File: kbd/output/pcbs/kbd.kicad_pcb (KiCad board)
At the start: 2 copper layers, 168.7 x 132.5 mm, 61 parts

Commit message: added mounting holes
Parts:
- added H1: , ceoloide:mounting_hole_plated, F.Cu at (207.5, 164.8)
- added H2: , ceoloide:mounting_hole_plated, F.Cu at (274.4, 180.3)
- added H3: , ceoloide:mounting_hole_plated, F.Cu at (140.5, 159.5)
- added H4: , ceoloide:mounting_hole_plated, F.Cu at (162.4, 60.3)
- added H5: , ceoloide:mounting_hole_plated, F.Cu at (212.1, 58.2)
- added H6: , ceoloide:mounting_hole_plated, F.Cu at (280.4, 77.4)
- added H7: , ceoloide:mounting_hole_plated, F.Cu at (229.8, 102.7)
- added H8: , ceoloide:mounting_hole_plated, F.Cu at (184.1, 100.5)
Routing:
- net (no net): track 856.2 -> 1280.0 mm
- net space_cluster: track 4.72 -> 0.00 mm, vias 1 -> 0
- net layer_cluster: track 4.72 -> 0.00 mm, vias 1 -> 0
- net outer_mod: track 4.72 -> 0.00 mm, vias 1 -> 0
- net outer_top: track 4.72 -> 0.00 mm, vias 1 -> 0
- net outer_num: track 4.72 -> 0.00 mm, vias 1 -> 0
- net outer_home: track 4.72 -> 0.00 mm, vias 1 -> 0
- net outer_bottom: track 4.72 -> 0.00 mm, vias 1 -> 0
- net middle_top: track 4.72 -> 0.00 mm, vias 1 -> 0
- net middle_num: track 4.72 -> 0.00 mm, vias 1 -> 0
- net middle_home: track 4.72 -> 0.00 mm, vias 1 -> 0
- net middle_bottom: track 4.72 -> 0.00 mm, vias 1 -> 0
- net ring_mod: track 4.72 -> 0.00 mm, vias 1 -> 0
- net ring_top: track 4.72 -> 0.00 mm, vias 1 -> 0
- net ring_home: track 4.72 -> 0.00 mm, vias 1 -> 0
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
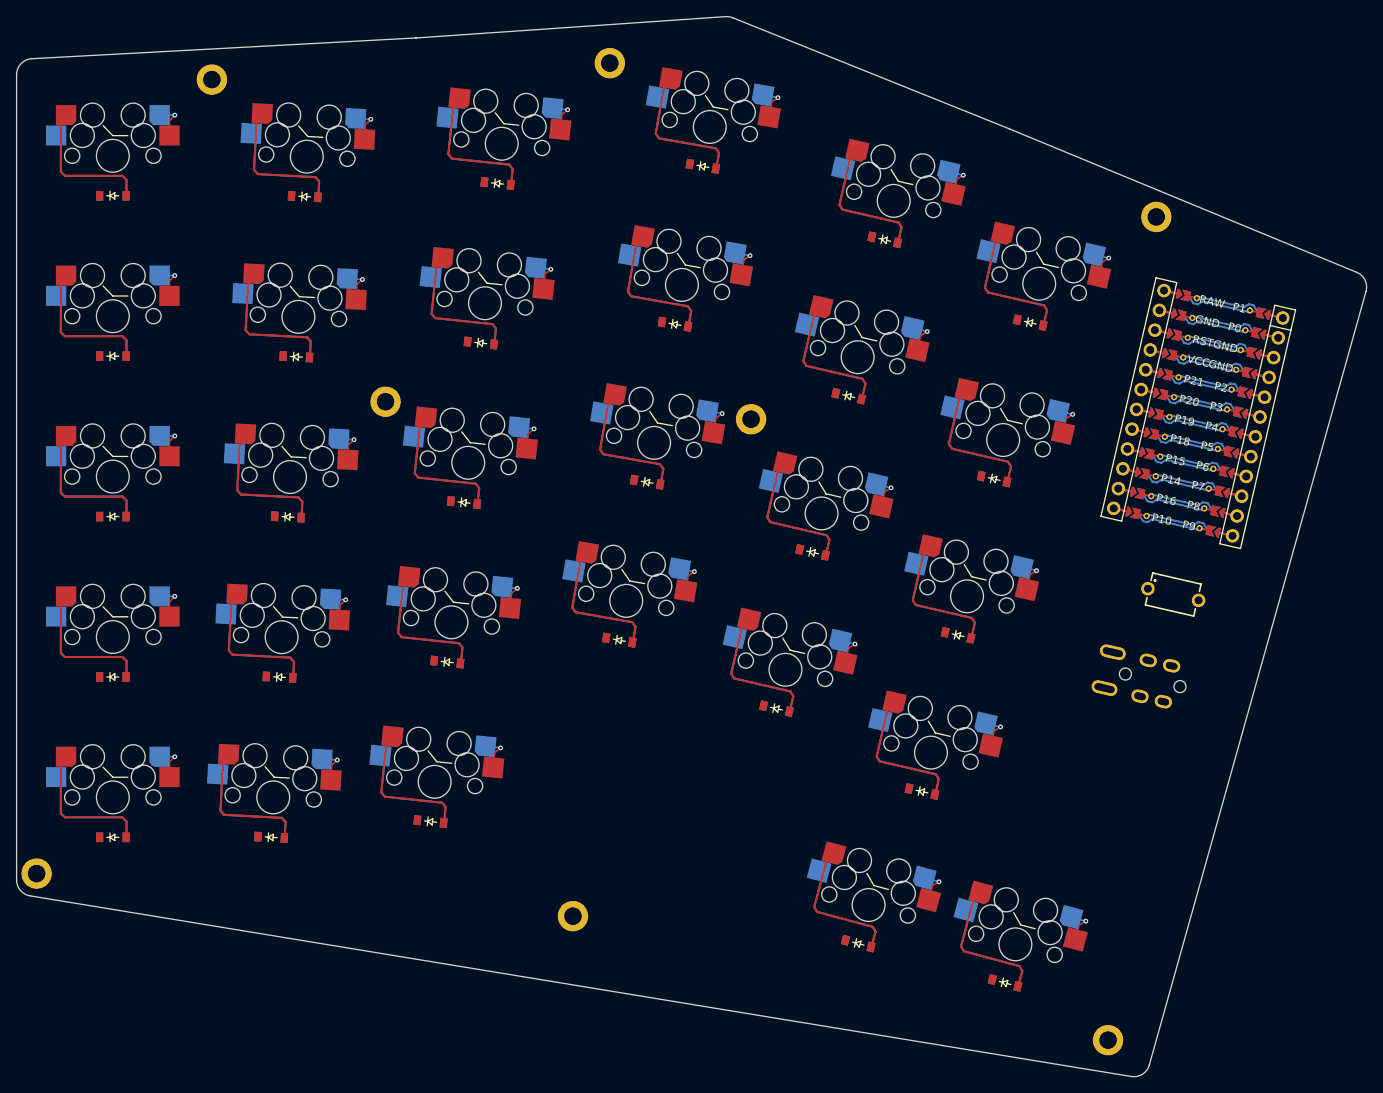
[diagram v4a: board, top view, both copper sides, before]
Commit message: fixed diodes
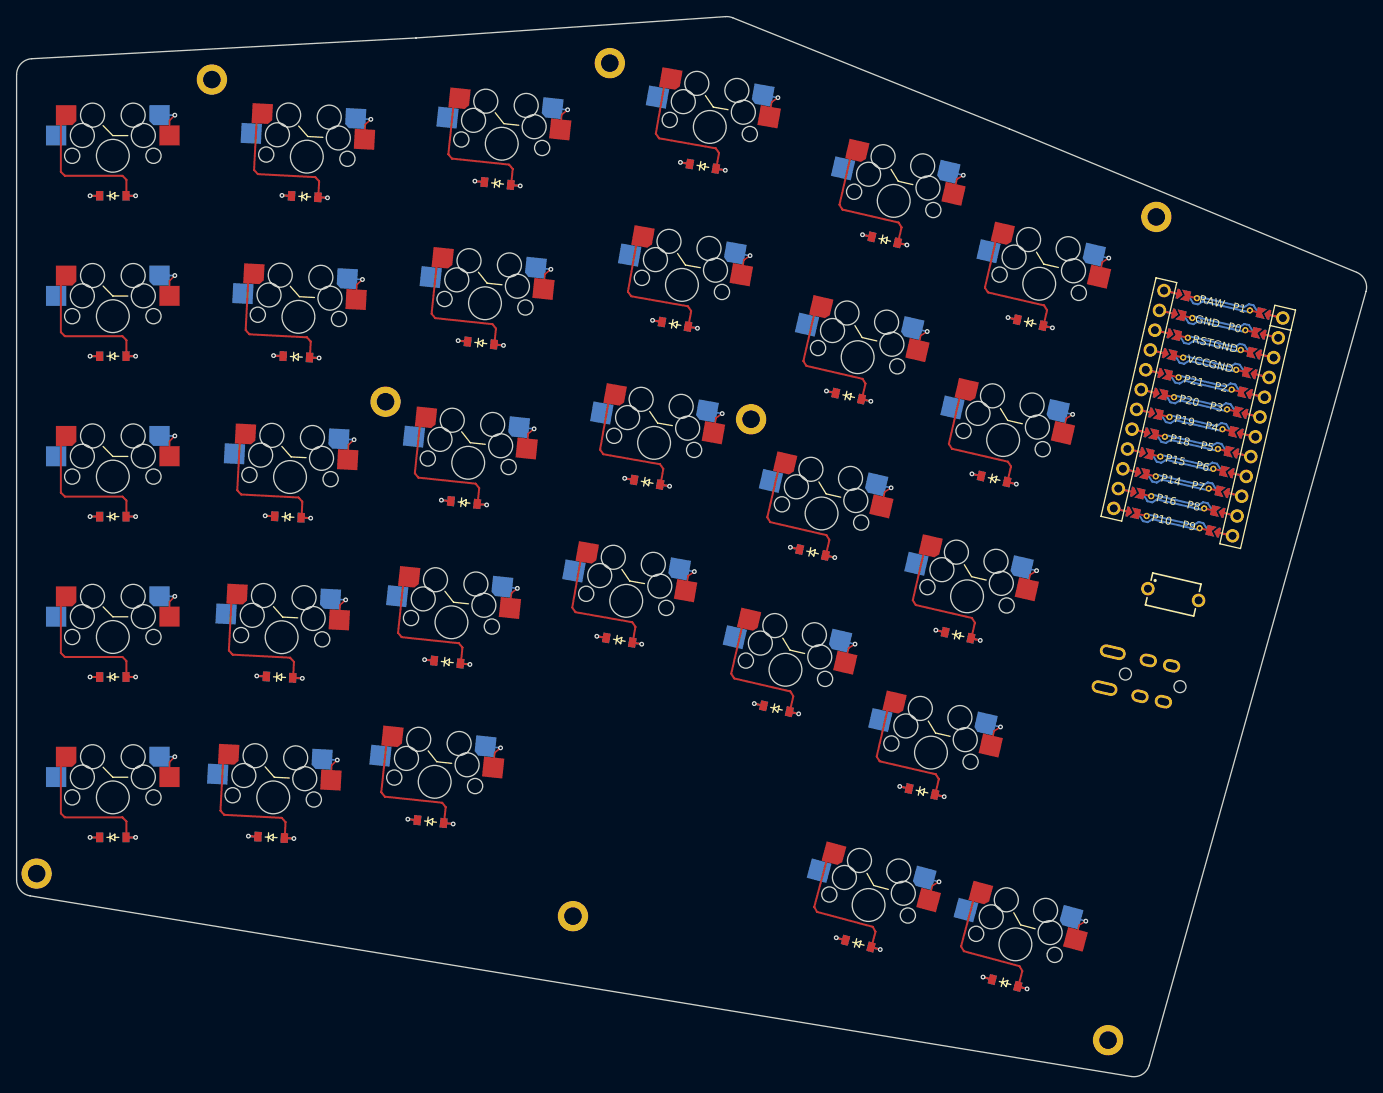
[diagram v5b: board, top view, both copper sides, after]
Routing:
- net (no net): track 1280.0 -> 856.2 mm
- net P14: track 0.00 -> 14.4 mm, vias 0 -> 6
- net P16: track 0.00 -> 14.4 mm, vias 0 -> 6
- net P18: track 0.00 -> 14.4 mm, vias 0 -> 6
- net P15: track 0.00 -> 14.4 mm, vias 0 -> 6
- net P10: track 0.00 -> 12.0 mm, vias 0 -> 5
- net pinky_top: track 0.00 -> 2.40 mm, vias 0 -> 1
- net pinky_num: track 0.00 -> 2.40 mm, vias 0 -> 1
- net pinky_home: track 0.00 -> 2.40 mm, vias 0 -> 1
- net pinky_mod: track 0.00 -> 2.40 mm, vias 0 -> 1
- net pinky_bottom: track 0.00 -> 2.40 mm, vias 0 -> 1
- net inner_bottom: track 0.00 -> 2.40 mm, vias 0 -> 1
- net index_top: track 0.00 -> 2.40 mm, vias 0 -> 1
- net index_num: track 0.00 -> 2.40 mm, vias 0 -> 1
- net index_home: track 0.00 -> 2.40 mm, vias 0 -> 1
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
